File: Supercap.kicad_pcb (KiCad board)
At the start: 4 copper layers, 116.8 x 70 mm, 73 parts, among them IC1 NCP5109ADR2G, IC2 NCP5109ADR2G, J1 XT30, J2 XT30, J2-J1 Conn_01x10, J3 Conn_01x01, J3-J1 Conn_01x10, J4 Conn_01x01, P7803B-1000R1 P7803B-1000, P7812B-1000R1 490-P7812B-1000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

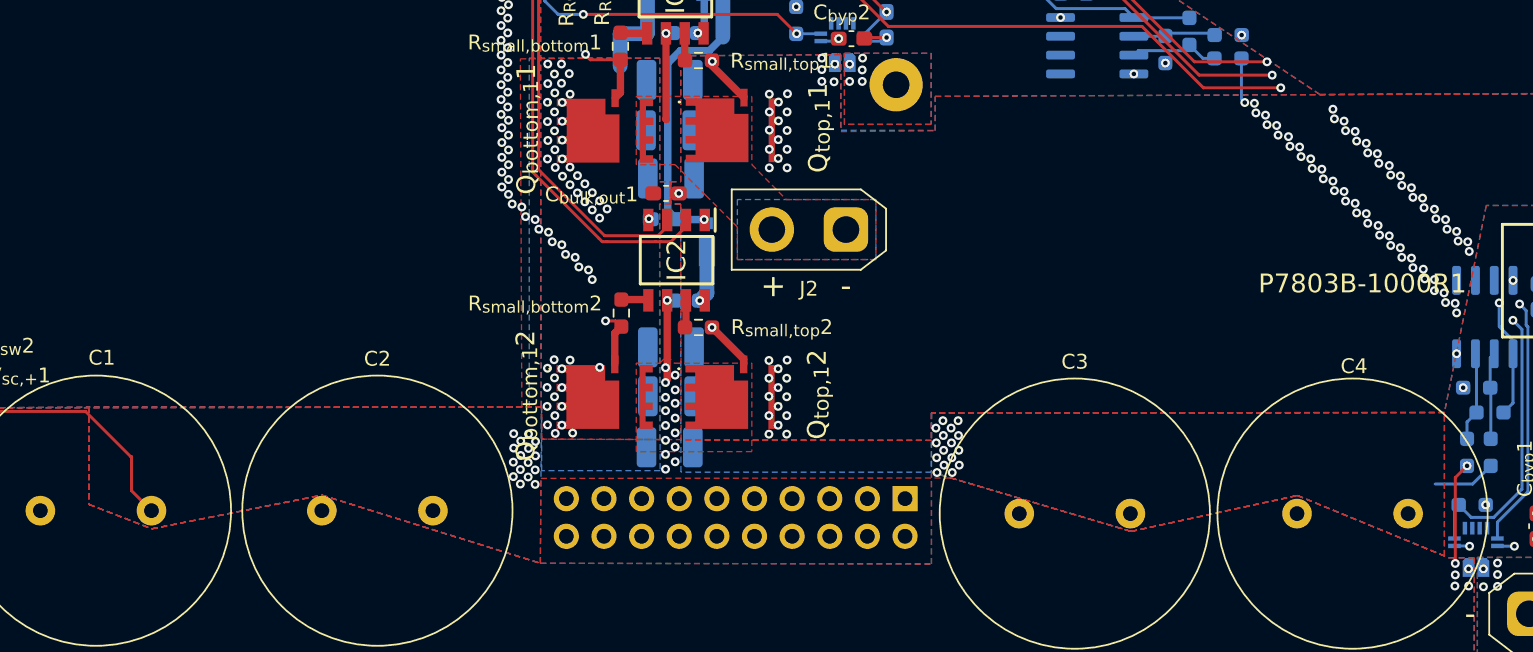
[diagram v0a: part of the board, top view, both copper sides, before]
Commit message: made corners better for switch nodes, hopefully
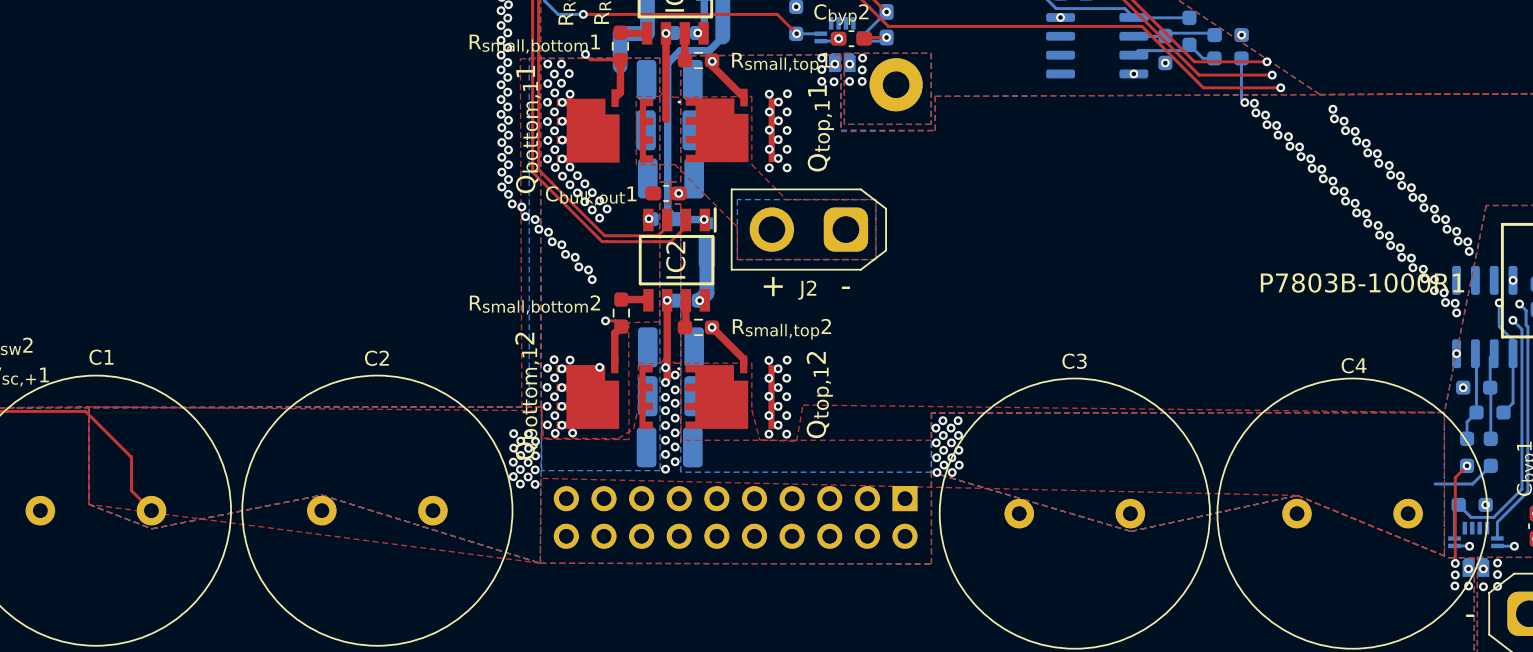
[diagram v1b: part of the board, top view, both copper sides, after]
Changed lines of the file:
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@@
 			(psa4output no)
 			(plot_black_and_white yes)
-			(plotinvisibletext no)
 			(sketchpadsonfab no)
 			(plotpadnumbers no)
@@
 			(pinfunction "BRIDGE")
 			(pintype "passive")
+			(teardrops
+				(best_length_ratio 0.5)
+				(max_length 1)
+				(best_width_ratio 1)
+				(max_width 2)
+				(curved_edges no)
+				(filter_ratio 0.9)
+				(enabled yes)
+				(allow_two_segments yes)
+				(prefer_zone_connections yes)
+			)
 		)
 		(pad "7" smd rect
@@
 			(pinfunction "BRIDGE")
 			(pintype "passive")
+			(teardrops
+				(best_length_ratio 0.5)
+				(max_length 1)
+				(best_width_ratio 1)
+				(max_width 2)
+				(curved_edges no)
+				(filter_ratio 0.9)
+				(enabled yes)
+				(allow_two_segments yes)
+				(prefer_zone_connections yes)
+			)
 		)
 		(pad "7" smd rect
@@
 			(thermal_gap 0.5)
 			(thermal_bridge_width 0.5)
+			(smoothing fillet)
+			(radius 1)
 		)
 		(polygon
 			(pts
 				(xy 77.660168 108.499446) (xy 78.385 108.499446) (xy 78.385 109.999446) (xy 77.649956 109.999446)
-				(xy 77.65 125.9) (xy 69.684135 125.874446) (xy 69.68325 123.700007) (xy 68.35 123.7) (xy 68.25 100.2)
-				(xy 77.655 100.149446)
+				(xy 77.649967 113.974585) (xy 77.649978 117.949723) (xy 75.56 118.01) (xy 75.59 125.9) (xy 69.684135 125.874446)
+				(xy 69.68325 123.700007) (xy 68.35 123.7) (xy 68.25 100.2) (xy 77.655 100.149446)
 			)
 		)
@@
 			(thermal_gap 0.5)
 			(thermal_bridge_width 0.5)
+			(smoothing fillet)
+			(radius 2)
 		)
 		(polygon
@@
 	)
 	(zone
+		(net 1)
+		(net_name "/Voltage Converter/V_{sw,2}")
+		(layer "F.Cu")
+		(name "$teardrop_padvia$")
+		(hatch none 0.1)
+		(priority 30000)
+		(attr
+			(teardrop
+				(type padvia)
+			)
+		)
+		(connect_pads yes
+			(clearance 0)
+		)
+		(min_thickness 0.0254)
+		(filled_areas_thickness no)
+		(fill yes
+			(thermal_gap 0.5)
+			(thermal_bridge_width 0.5)
+			(island_removal_mode 1)
+			(island_area_min 10)
+		)
+		(polygon
+			(pts
+				(xy 77.909723 117.615223) (xy 78.409723 117.615223) (xy 78.509723 117.265223) (xy 78.159723 116.501723)
+				(xy 77.809723 117.265223)
+			)
+		)
+	)
+	(zone
+		(net 4)
+		(net_name "/Voltage Converter/V_{sw,1}")
+		(layer "F.Cu")
+		(name "$teardrop_padvia$")
+		(hatch none 0.1)
+		(priority 30001)
+		(attr
+			(teardrop
+				(type padvia)
+			)
+		)
+		(connect_pads yes
+			(clearance 0)
+		)
+		(min_thickness 0.0254)
+		(filled_areas_thickness no)
+		(fill yes
+			(thermal_gap 0.5)
+			(thermal_bridge_width 0.5)
+			(island_removal_mode 1)
+			(island_area_min 10)
+		)
+		(polygon
+			(pts
+				(xy 77.83 99.594223) (xy 78.33 99.594223) (xy 78.43 99.244223) (xy 78.08 98.480723) (xy 77.73 99.244223)
+			)
+		)
+	)
+	(zone
 		(net 3)
 		(net_name "GNDPWR")
@@
 			(thermal_bridge_width 0.5)
 			(smoothing fillet)
-			(radius 2)
+			(radius 1)
 		)
 		(polygon
@@
 				(xy 83.875 107.339446) (xy 86.2 109.7) (xy 92.25 109.7) (xy 92.25 113.75) (xy 82.9 113.75) (xy 82.9 111.55)
 				(xy 80.794723 109.444723) (xy 78.689446 107.339446) (xy 76.075 107.339446) (xy 76.075 102.739446)
-				(xy 83.875 102.739446)
+				(xy 77.64 102.739446) (xy 78.05 102.228859) (xy 78.56 102.800392) (xy 83.875 102.739446)
 			)
 		)
@@
 			(thermal_gap 0.5)
 			(thermal_bridge_width 0.5)
+			(smoothing fillet)
+			(radius 2)
 		)
 		(polygon
 			(pts
-				(xy 83.875 126.714446) (xy 76.075 126.714446) (xy 76.075 120.739446) (xy 77.65 120.75) (xy 78.15 120.25)
-				(xy 78.65 120.75) (xy 83.875 120.739446)
+				(xy 83.875 123.883401) (xy 84.411281 125.928698) (xy 86.9 126.025249) (xy 87.328935 123.57) (xy 130.625 124.075)
+				(xy 130.63 133.76) (xy 120.7 129.675) (xy 69.635069 128.522035) (xy 69.6 134.25) (xy 39.125 130.275)
+				(xy 39.125 123.7) (xy 69.680797 123.95) (xy 69.81 125.807263) (xy 74.837263 125.836439) (xy 75.900104 125.18)
+				(xy 76.19 123.856491) (xy 76.21 120.75) (xy 77.759997 120.747866) (xy 78.159996 120.12) (xy 78.649995 120.74664)
+				(xy 83.875 120.739446)
 			)
 		)
 	)
 	(zone
-		(net 1)
-		(net_name "/Voltage Converter/V_{sw,2}")
-		(layers "F.Cu" "In1.Cu" "In2.Cu")
+		(net 4)
+		(net_name "/Voltage Converter/V_{sw,1}")
+		(layer "B.Cu")
 		(hatch edge 0.5)
-		(priority 5)
+		(priority 8)
 		(connect_pads yes
 			(clearance 0.5)
@@
 			(thermal_bridge_width 0.5)
 			(smoothing fillet)
-			(radius 2)
+			(radius 3)
 		)
 		(polygon
 			(pts
-				(xy 39.125 123.7) (xy 39.125 130.275) (xy 43.375 131.925) (xy 54.85 129.65) (xy 69.6 134.25) (xy 69.635069 128.522035)
-				(xy 97.330753 128.495186) (xy 109.474828 132.1) (xy 120.7 129.675) (xy 130.63 133.76) (xy 130.625 124.075)
-				(xy 96 124.125) (xy 95.996799 125.949446) (xy 69.684135 125.874446) (xy 69.675 123.7)
+				(xy 82.9 113.75) (xy 92.25 113.75) (xy 92.25 109.7) (xy 82.9 109.7)
 			)
 		)
 	)
 	(zone
-		(net 4)
-		(net_name "/Voltage Converter/V_{sw,1}")
+		(net 7)
+		(net_name "/Housekeeping/+12V")
 		(layer "B.Cu")
-		(hatch edge 0.5)
-		(priority 8)
+		(name "$teardrop_track$")
+		(hatch none 0.1)
+		(priority 30000)
+		(attr
+			(teardrop
+				(type track_end)
+			)
+		)
 		(connect_pads yes
-			(clearance 0.5)
+			(clearance 0)
 		)
-		(min_thickness 0.25)
+		(min_thickness 0.0254)
 		(filled_areas_thickness no)
 		(fill yes
 			(thermal_gap 0.5)
 			(thermal_bridge_width 0.5)
-			(smoothing fillet)
-			(radius 3)
+			(island_removal_mode 1)
+			(island_area_min 10)
 		)
 		(polygon
 			(pts
-				(xy 82.9 113.75) (xy 92.25 113.75) (xy 92.25 109.7) (xy 82.9 109.7)
+				(xy 81.03891 99.257536) (xy 81.392464 99.61109) (xy 82.193785 99.149735) (xy 81.916707 98.733293)
+				(xy 81.500265 98.456215)
 			)
 		)

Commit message: cleaned up sections to be repositioned
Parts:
- moved C3 103.9 mm to (-1.97, 130.9)
- moved C4 103.9 mm to (16.8, 130.9)
- moved R_{RC}1 68.3 mm to (123.7, 49.0)
- moved R_{RC}2 68.3 mm to (126.2, 49.0)
- moved C_{RC}1 61.8 mm to (117.6, 53.7)
- moved C_{RC}2 61.8 mm to (120.1, 53.8)
- moved C_{byp}2 59.1 mm to (128.8, 53.7)
- moved C_{l}2 59.1 mm to (131.2, 52.8)
- moved J4 59.1 mm to (131.8, 56.8)
- moved U4 59.1 mm to (128.2, 54.1)
- moved C_{l}1 55.1 mm to (124.3, 54.0)
- moved C_{smooth}3 52.3 mm to (134.7, 52.3), turned to 90 degrees
- moved R_{pu}2 48.1 mm to (118.5, 61.4)
- moved C_{smooth}2 41.5 mm to (122.5, 57.9)
- moved R_{sens,bottom}2 41.5 mm to (130.3, 60.4)
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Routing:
- net /Control/V_{sc,sens}: track 82.9 -> 8.05 mm, vias 4 -> 1
- net /Control/I_L: track 85.4 -> 18.8 mm, vias 3 -> 1
- net /Housekeeping/+12V: track 84.2 -> 26.9 mm
- net /Control/F_L: track 81.5 -> 24.7 mm, vias 3 -> 1
- net /Control/PA25: track 52.7 -> 0.44 mm
- net /Voltage Converter/V_{sw,1}: track 59.5 -> 7.83 mm
- net /Voltage Converter/LO_DRV_{2}: track 54.4 -> 4.73 mm, vias 1 -> 0
- net /Voltage Converter/HI_DRV_{2}: track 57.1 -> 8.00 mm
- net /Control/PB9: track 44.7 -> 0.44 mm
- net /Control/V_{bat,sens}: track 42.4 -> 3.76 mm, vias 3 -> 0
- net /Voltage Converter/HI_DRV_{1}: track 44.0 -> 5.47 mm, vias 1 -> 0
- net /Control/F_bat: track 34.4 -> 0.00 mm, vias 2 -> 0
- net /Voltage Converter/LO_DRV_{1}: track 36.6 -> 4.73 mm, vias 1 -> 0
- net GND: track 25.7 -> 1.03 mm, vias 12 -> 8
- net /Control/+3V3: track 28.4 -> 4.22 mm, vias 11 -> 8
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- removed copper zone on In1.Cu, net /Control/+3V3
- removed copper zone on B.Cu, net /Control/I_{bat,out+}
- removed copper zone on F.Cu, net /Control/I_{bat,out+}
- removed copper zone on In1.Cu, net /Control/I_{bat,out+}
- removed copper zone on In2.Cu, net /Control/I_{bat,out+}
- removed copper zone on B.Cu, net /Control/V_{sc,+}
- removed copper zone on F.Cu, net /Control/V_{sc,+}
- removed copper zone on In1.Cu, net /Control/V_{sc,+}
- removed copper zone on In2.Cu, net /Control/V_{sc,+}
- removed copper zone on B.Cu, net /Voltage Converter/V_{sw,1}
- removed copper zone on B.Cu, net /Voltage Converter/V_{sw,2}
- removed copper zone on F.Cu, net /Voltage Converter/V_{sw,2}
- removed copper zone on In1.Cu, net /Voltage Converter/V_{sw,2}
- removed copper zone on In2.Cu, net /Voltage Converter/V_{sw,2}
- removed copper zone on In2.Cu, net GND
- removed copper zone on B.Cu, net Net-(J4-Pin_1)
- removed copper zone on F.Cu, net Net-(J4-Pin_1)
- removed copper zone on In1.Cu, net Net-(J4-Pin_1)
- removed copper zone on In2.Cu, net Net-(J4-Pin_1)

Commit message: need to see other board
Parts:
- moved C_{RC}2 74.4 mm to (106.2, 126.9)
- moved C_{byp}2 74.4 mm to (114.9, 126.8)
- moved C_{l}2 74.4 mm to (117.3, 125.9)
- moved J4 74.4 mm to (117.9, 129.9)
- moved R_{sens,bottom}1 74.4 mm to (114.8, 134.7)
- moved R_{sens,bottom}2 74.4 mm to (116.4, 133.5)
- moved R_{sens,top}2 74.4 mm to (119.0, 133.8)
- moved U2 74.4 mm to (110.2, 134.5)
- moved C_{RC}1 74.4 mm to (103.7, 126.8)
- moved C_{l}1 74.4 mm to (110.5, 127.1)
- moved C_{smooth}2 74.4 mm to (108.6, 131.0)
- moved C_{smooth}3 74.4 mm to (120.8, 125.4)
- moved R_{RC}1 74.4 mm to (109.8, 122.1)
- moved R_{RC}2 74.4 mm to (112.3, 122.1)
- moved R_{sens,top}1 74.4 mm to (119.0, 135.3)
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
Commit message: need to pu v1 to make copy on other desktop
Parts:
- moved U6 103.3 mm to (269.7, 44.9)
- moved J1 75.4 mm to (176.2, 98.8)
- moved C_{smooth}6 68.2 mm to (172.2, 120.3), turned to 90 degrees
- moved D_{b}1 65.8 mm to (170.8, 123.3), turned to 0 degrees
- moved IC1 64.2 mm to (169.4, 121.3), turned to 180 degrees
- moved C_{RC}2 63.7 mm to (151.7, 82.3)
- moved C_{byp}2 63.7 mm to (160.4, 82.2)
- moved J4 63.7 mm to (163.4, 85.3)
- moved R_{RC}1 63.7 mm to (155.3, 77.5)
- moved R_{sens,bottom}1 63.7 mm to (160.3, 90.1)
- moved R_{sens,bottom}2 63.7 mm to (161.9, 88.9)
- moved R_{sens,top}2 63.7 mm to (164.6, 89.2)
- moved U2 63.7 mm to (155.7, 89.9)
- moved C_{RC}1 63.7 mm to (149.2, 82.2)
- moved C_{l}1 63.7 mm to (155.9, 82.5)
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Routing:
- net /Voltage Converter/V_{sw,2}: track 32.0 -> 11.6 mm
- added copper zone on B.Cu, net GND
- added copper zone on F.Cu, net GND
- added copper zone on In1.Cu, net GND
- added copper zone on In2.Cu, net GND
- removed copper zone on B.Cu, net /Control/I_{L,out+}
- removed copper zone on In1.Cu, net /Control/I_{L,out+}
- removed copper zone on In2.Cu, net /Control/I_{L,out+}
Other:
- board size 116.8 x 70 mm -> 151.8 x 70 mm

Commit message: im so bad at this :skull Vsc+ pour boutta go crazy, the mspm0 pin buses too, idk if i even got what i did right lmao but ill figure it out later
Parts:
- C_{byp}2, R_{RC}2: moved to B.Cu
- moved GNDPWR1 125.5 mm to (158.0, 160.2)
- moved GNDPWR2 125.5 mm to (155.4, 160.2)
- moved HI_{DRV}1 125.5 mm to (174.6, 160.1)
- moved HI_{DRV}2 125.5 mm to (167.1, 160.1)
- moved LO_{DRV}1 125.5 mm to (172.1, 160.1)
- moved LO_{DRV}2 125.5 mm to (164.6, 160.1)
- moved V_{sw}1 125.5 mm to (169.6, 160.1)
- moved J3-J1 37.6 mm to (138.4, 90.5)
- moved C_{RC}1 28.4 mm to (177.3, 86.3)
- moved R_{RC}1 20.1 mm to (174.9, 81.9), turned to 180 degrees
- moved C_{l}1 16.2 mm to (169.3, 91.8), turned to 0 degrees
- moved R_{pu}2 14.8 mm to (164.5, 86.2), turned to 180 degrees
- moved R_{RC}2 12.8 mm to (164.8, 88.2), turned to 180 degrees
- moved C_{RC}2 11.3 mm to (162.0, 87.0), turned to 90 degrees
- moved U4 10.5 mm to (169.2, 87.2), turned to 180 degrees
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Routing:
- net /Control/F_L: track 24.7 -> 2.39 mm, vias 1 -> 0
- net /Control/I_L: track 18.8 -> 7.74 mm, vias 1 -> 0
- net GND: track 1.03 -> 8.17 mm, vias 8 -> 6
- net Net-(U2A-+): track 6.10 -> 11.9 mm
- net /Control/F_bat: track 0.00 -> 4.35 mm
- net /Voltage Converter/V_{sw,2}: track 11.6 -> 7.37 mm
- net Net-(J4-Pin_1): track 0.00 -> 3.51 mm
- net /Control/V_{bat,sens}: track 3.76 -> 7.21 mm
- net /Control/I_{bat,out+}: track 0.00 -> 2.62 mm, vias 30 -> 29
- net /Control/V_{sc,sens}: track 8.05 -> 6.10 mm
- net /Control/+3V3: track 4.22 -> 5.58 mm, vias 8 -> 10
- net Net-(U2A--): track 5.59 -> 6.59 mm
- net /Control/I_bat: track 2.11 -> 2.81 mm, vias 1 -> 0
- added copper zone on F.Cu, net /Control/+3V3
- added copper zone on In1.Cu, net /Control/+3V3
- added copper zone on B.Cu, net /Control/I_{L,out+}
- added copper zone on In1.Cu, net /Control/I_{L,out+}
- added copper zone on In2.Cu, net /Control/I_{L,out+}

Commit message: getting paranoid that kicads gonna crash: moved current sense IC and inductor pad assoc. drew rest of main pours for cap charging, gndpwr, etc
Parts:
- J1: moved to B.Cu
- U3: moved to F.Cu
- moved U3 61.8 mm to (116.2, 117.7), turned to -90 degrees
- moved J1 57.5 mm to (121.5, 116.6)
- moved J2-J1 33.2 mm to (138.4, 133.7)
- moved U6 25.8 mm to (243.9, 46.5)
- moved R2 8.89 mm to (171.0, 96.0)
- moved R1 8.89 mm to (169.4, 96.0)
- moved R_{sens,top}1 6.11 mm to (167.6, 96.0), turned to 90 degrees
- moved R_{sens,top}2 0.42 mm to (165.7, 96.1)
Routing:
- net Net-(U1A-+): track 6.04 -> 15.7 mm
- net Net-(U1A--): track 5.87 -> 15.5 mm
- net GND: track 8.17 -> 0.00 mm, vias 6 -> 5
- net /Control/I_{bat,out+}: track 2.62 -> 10.5 mm
- net /Control/I_L: track 7.74 -> 0.00 mm
- net /Control/V_{sc,+}: track 8.91 -> 2.00 mm, vias 6 -> 5
- net /Housekeeping/+12V: track 26.9 -> 32.6 mm
- net Net-(U2A-+): track 11.9 -> 16.3 mm
- net /Control/F_L: track 2.39 -> 0.00 mm
- net /Control/+3V3: track 5.58 -> 4.42 mm, vias 10 -> 9
- net /Control/I_{L,out+}: vias 5 -> 4
- added copper zone on B.Cu, net /Control/I_{bat,out+}
- added copper zone on F.Cu, net /Control/I_{bat,out+}
- added copper zone on In1.Cu, net /Control/I_{bat,out+}
- added copper zone on In2.Cu, net /Control/I_{bat,out+}
- added copper zone on B.Cu, net /Control/V_{sc,+}
- added copper zone on F.Cu, net /Control/V_{sc,+}
- added copper zone on In1.Cu, net /Control/V_{sc,+}
- added copper zone on In2.Cu, net /Control/V_{sc,+}
- added copper zone on B.Cu, net /Voltage Converter/V_{sw,2}
- added copper zone on F.Cu, net /Voltage Converter/V_{sw,2}
- added copper zone on In1.Cu, net /Voltage Converter/V_{sw,2}
- added copper zone on In2.Cu, net /Voltage Converter/V_{sw,2}
